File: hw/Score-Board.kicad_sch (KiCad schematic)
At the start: 102 parts, among them J1 Conn_01x03, J2 Conn_01x04, J3 Barrel_Jack, J4 Conn_01x04, J5 Conn_01x02, J6 DB25_Receptacle_MountingHoles, J7 Conn_01x10, J8 Conn_01x14, Q1 2N3905, Q10 2N3904, Q11 2N3905, Q12 2N3904, Q13 2N3905, Q14 2N3904, Q15 2N3905, Q16 2N3904, Q17 2N3905, Q18 2N3904, Q19 2N3905, Q2 2N3904, Q20 2N3904, Q21 2N3905, Q22 2N3904, Q3 2N3904, Q4 2N3904, Q5 2N3904, Q6 2N3904, Q7 2N3904, Q8 2N3904, Q9 2N3904, SW1 RESET, SW2 NETWORK, SW3 INPUT-SW, U1 PicoW, U2 E18-MS1-PCB, U3 TSOP382xx, U4 TSOP382xx

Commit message: Schematic complete v0.1. Ready for layout.
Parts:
- removed J5: Conn_01x02, symbol Connector_Generic:Conn_01x02
- removed R26, R27: 150, symbol Device:R_Small_US
- added C4, C5: 1.0uF, symbol Device:C
- added D2: DIODE SCHOTTKY 50V 200MA DO35, symbol Device:D_Schottky
- added J2: J-V12, symbol Connector_Generic:Conn_01x02
- added J3: J-VSYS, symbol Connector_Generic:Conn_01x02
- added J4: J-V3.3, symbol Connector_Generic:Conn_01x02
- added J5: MicroSD-Socket, symbol Connector:Micro_SD_Card_Det1
- added R27, R44: 150, symbol AES_Library:R_PWRSRC
- added TP1: Conn_01x01, symbol Connector_Generic:Conn_01x01
- added U5: MCP1702-5002E, Package_TO_SOT_THT:TO-92_Inline, symbol Regulator_Linear:MCP1700x-500xxTO
- renumbered J3 to J1, J7 to J10, J8 to J11, J1 to J6, J2 to J7, J4 to J8, J6 to J9
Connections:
- net +12V: now also R11.1, C4.1, J2.2 (Pin_2), U5.2 (VI)
- net +3.3V: now also J4.2 (Pin_2), J5.4 (VDD), R27.1 (I), R44.1 (I)
- net DD.IND: now also LED10.2 (A)
- net GND: now also J6.1 (Pin_1), C4.2, C5.2, J2.1 (Pin_1), J3.1 (Pin_1), J5.10 (SHIELD), J5.6 (VSS), U5.1 (GND); no longer J6.3 (Pin_3), LED2.1 (K), LED3.1 (K), U1.31 (GPIO26_ADC0), U2.12 (RUN_LED), U2.13 (NWK_LED)
- net SC_TX: now also J6.3 (Pin_3); no longer J6.1 (Pin_1)
- net SE.E: now also J5.5 (CLK)
- net SE.F: now also J5.3 (CMD)
- net SE.G: now also J5.7 (DAT0)
- net VIR.B: now reaches C2.2, U4.3 (Vs)
- net VIR.B: now also R27.2 (O)
- net VSYS: now reaches U1.39 (VSYS)
- net VSYS: now also D2.1 (K), J3.2 (Pin_2), J4.1 (Pin_1)
- net VIR.A: now reaches C3.2, U3.3 (Vs)
- net VIR.A: now also R44.2 (O)
- new net: LED3.1 (K), U2.13 (NWK_LED)
- new net: LED2.1 (K), U2.12 (RUN_LED)
- new net +5V: C5.1, D2.2 (A), TP1.1 (Pin_1), U5.3 (VO)
- new net SD_CS-: J5.2 (DAT3/CD), U1.31 (GPIO26_ADC0)
- no-connect marks 13 -> 20
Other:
- note added: "IR Receiver A"
- note added: "IR Receiver B"
- note removed: "SEGMENT DRIVE BUS (A-G,P)"
- note removed: "SEGMENT ENABLE BUS (A-G,P)"
- moved on the sheet: BZ1, C1, C2, C3, D1, J1, J6, J7, J8, LED1, LED2, LED3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

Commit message: Schematic updated with 3 digit boards
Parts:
- removed DIG1, DIG2, DIG3, DIG4: WJLEDS40012TUR11, Display_7Segment:SA15-11xxx, symbol AES_Library:WJ-LEDS40012TUR11
- removed DIG5, DIG6: WJLEDS18012TUR11, Display_7Segment:SA15-11xxx, symbol AES_Library:WJ-LEDS18012TUR11
- removed J10: Conn_01x10, symbol Connector_Generic:Conn_01x10
- removed J11: Conn_01x14, symbol Connector_Generic:Conn_01x14
- removed LED10: IND-B3, symbol Device:LED
- removed LED11: IND-B4, symbol Device:LED
- removed LED4: IND-A1, symbol Device:LED
- removed LED5: IND-A2, symbol Device:LED
- removed LED6: IND-A3, symbol Device:LED
- removed LED7: IND-A4, symbol Device:LED
- removed LED8: IND-B1, symbol Device:LED
- removed LED9: IND-B2, symbol Device:LED
- removed R28, R29, R30, R31, R32, R33, R34, R36, R37, R38, R39, R40, R41, R42: 150, symbol Device:R_Small_US
- removed R35, R43: 0, symbol Device:R_Small_US
- added H1, H2, H3, H4: MountingHole, MountingHole:MountingHole_3.2mm_M3, symbol Mechanical:MountingHole
- added J14: Conn_02x09_Odd_Even, symbol Connector_Generic:Conn_02x09_Odd_Even
- added J14: Screw_Terminal_01x02, symbol Connector:Screw_Terminal_01x02
- BZ1: footprint (none) -> MountingHole:MountingHole_3.2mm_M3
- C1: footprint (none) -> Capacitor_THT:CP_Radial_D8.0mm_P3.50mm
- C2: renamed from C4; footprint (none) -> Capacitor_THT:CP_Radial_D5.0mm_P2.00mm
- C3: renamed from C5; footprint (none) -> Capacitor_THT:CP_Radial_D5.0mm_P2.00mm
- C4: renamed from C3; footprint (none) -> Capacitor_THT:CP_Radial_D5.0mm_P2.00mm
- C5: renamed from C2; footprint (none) -> Capacitor_THT:CP_Radial_D5.0mm_P2.00mm
- D2: footprint (none) -> Diode_THT:D_DO-35_SOD27_P10.16mm_Horizontal
- J1: footprint (none) -> AES_Library:CUI_PJ-037B
- J10: renamed from J9; footprint (none) -> Connector_Dsub:DSUB-25_Female_Horizontal_P2.77x2.54mm_EdgePinOffset9.40mm
- J2: renamed from J7; footprint (none) -> Connector_PinHeader_2.54mm:PinHeader_1x04_P2.54mm_Vertical
- J3: renamed from J6; footprint (none) -> Connector_PinHeader_2.54mm:PinHeader_1x03_P2.54mm_Vertical
- J4: renamed from J8; footprint (none) -> Connector_PinHeader_2.54mm:PinHeader_1x04_P2.54mm_Vertical
- J5: footprint (none) -> AES_Library:GCT_MEM2075-00-140-01-A
- J6: renamed from J2; footprint (none) -> Connector_PinHeader_2.54mm:PinHeader_1x02_P2.54mm_Vertical
- J7: renamed from J3; footprint (none) -> Connector_PinHeader_2.54mm:PinHeader_1x02_P2.54mm_Vertical
- J8: renamed from J4; footprint (none) -> Connector_PinHeader_2.54mm:PinHeader_1x02_P2.54mm_Vertical
- LED1, LED2, LED3: footprint (none) -> LED_THT:LED_D5.0mm-3
- R1: renamed from R44; footprint (none) -> Resistor_THT:R_Axial_DIN0207_L6.3mm_D2.5mm_P10.16mm_Horizontal
- R10: renamed from R13; footprint (none) -> Resistor_THT:R_Axial_DIN0207_L6.3mm_D2.5mm_P10.16mm_Horizontal
- R11: renamed from R14; footprint (none) -> Resistor_THT:R_Axial_DIN0207_L6.3mm_D2.5mm_P10.16mm_Horizontal
- R12: renamed from R15; footprint (none) -> Resistor_THT:R_Axial_DIN0207_L6.3mm_D2.5mm_P10.16mm_Horizontal
- R13: renamed from R16; footprint (none) -> Resistor_THT:R_Axial_DIN0207_L6.3mm_D2.5mm_P10.16mm_Horizontal
- R14: renamed from R17; footprint (none) -> Resistor_THT:R_Axial_DIN0207_L6.3mm_D2.5mm_P10.16mm_Horizontal
- R15: renamed from R18; footprint (none) -> Resistor_THT:R_Axial_DIN0207_L6.3mm_D2.5mm_P10.16mm_Horizontal
- R16: renamed from R19; footprint (none) -> Resistor_THT:R_Axial_DIN0207_L6.3mm_D2.5mm_P10.16mm_Horizontal
- R17: renamed from R20; footprint (none) -> Resistor_THT:R_Axial_DIN0207_L6.3mm_D2.5mm_P10.16mm_Horizontal
- R18: renamed from R24; footprint (none) -> Resistor_THT:R_Axial_DIN0207_L6.3mm_D2.5mm_P10.16mm_Horizontal
- R19: renamed from R25; footprint (none) -> Resistor_THT:R_Axial_DIN0207_L6.3mm_D2.5mm_P10.16mm_Horizontal
- R2: renamed from R27; footprint (none) -> Resistor_THT:R_Axial_DIN0207_L6.3mm_D2.5mm_P10.16mm_Horizontal
- R20: renamed from R3; footprint (none) -> Resistor_THT:R_Axial_DIN0207_L6.3mm_D2.5mm_P10.16mm_Horizontal
- R3: renamed from R21; footprint (none) -> Resistor_THT:R_Axial_DIN0207_L6.3mm_D2.5mm_P10.16mm_Horizontal
- R33: renamed from R4; footprint (none) -> Resistor_THT:R_Axial_DIN0207_L6.3mm_D2.5mm_P10.16mm_Horizontal
- R34: renamed from R5; footprint (none) -> Resistor_THT:R_Axial_DIN0207_L6.3mm_D2.5mm_P10.16mm_Horizontal
- R39: renamed from R6; footprint (none) -> Resistor_THT:R_Axial_DIN0207_L6.3mm_D2.5mm_P10.16mm_Horizontal
- R4: renamed from R22; footprint (none) -> Resistor_THT:R_Axial_DIN0207_L6.3mm_D2.5mm_P10.16mm_Horizontal
- R40: renamed from R7; footprint (none) -> Resistor_THT:R_Axial_DIN0207_L6.3mm_D2.5mm_P10.16mm_Horizontal
- R41: renamed from R8; footprint (none) -> Resistor_THT:R_Axial_DIN0207_L6.3mm_D2.5mm_P10.16mm_Horizontal
- R42: renamed from R9; footprint (none) -> Resistor_THT:R_Axial_DIN0207_L6.3mm_D2.5mm_P10.16mm_Horizontal
- R43: renamed from R10; footprint (none) -> Resistor_THT:R_Axial_DIN0207_L6.3mm_D2.5mm_P10.16mm_Horizontal
- R5: renamed from R23; footprint (none) -> Resistor_THT:R_Axial_DIN0207_L6.3mm_D2.5mm_P10.16mm_Horizontal
- R6: renamed from R1; footprint (none) -> Resistor_THT:R_Axial_DIN0207_L6.3mm_D2.5mm_P10.16mm_Horizontal
- R7: renamed from R2; footprint (none) -> Resistor_THT:R_Axial_DIN0207_L6.3mm_D2.5mm_P10.16mm_Horizontal
- R8: renamed from R11; footprint (none) -> Resistor_THT:R_Axial_DIN0207_L6.3mm_D2.5mm_P10.16mm_Horizontal
- R9: renamed from R12; footprint (none) -> Resistor_THT:R_Axial_DIN0207_L6.3mm_D2.5mm_P10.16mm_Horizontal
- SW1, SW2, SW3: footprint (none) -> AES_Library:SW_TL1100F160Q
- TP1: footprint (none) -> Connector_PinHeader_2.54mm:PinHeader_1x01_P2.54mm_Vertical
- U1: footprint RPi_PicoW:RPi_Pico_SMD_TH -> AES_Library:RPi_PicoW_SMD_TH
- renumbered Q2 to Q1, Q13 to Q10, Q15 to Q11, Q17 to Q12, Q19 to Q13, Q21 to Q14, Q3 to Q15, Q4 to Q16, Q5 to Q17, Q6 to Q18, Q7 to Q19, Q12 to Q2, Q8 to Q20, Q9 to Q21, Q10 to Q22, Q14 to Q3, Q16 to Q4, Q18 to Q5, Q20 to Q6, Q22 to Q7, Q1 to Q8, Q11 to Q9
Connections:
- net +12V: now also J14.2 (Pin_2)
- net +3.3V: no longer U1.35 (ADC_VREF)
- net DD.A01: now also J10.20 (P20), J14.4 (Pin_4); no longer J10.7
- net DD.A10: now also J10.7, J14.2 (Pin_2); no longer J10.20 (P20)
- net DD.B01: now also J10.21 (P21), J14.8 (Pin_8); no longer J10.8
- net DD.B10: now also J10.8, J14.6 (Pin_6); no longer J10.21 (P21)
- net DD.C01: now also J10.22 (P22), J14.12 (Pin_12); no longer J10.9
- net DD.C10: now also J10.9, J14.10 (Pin_10); no longer J10.22 (P22)
- net DD.IND: now also J14.14 (Pin_14), J14.16 (Pin_16)
- net GND: now also J14.1 (Pin_1), J14.1 (Pin_1), J14.18 (Pin_18); no longer J10.13
- net SD.A: now also J14.3 (Pin_3)
- net SD.B: now also J14.5 (Pin_5)
- net SD.C: now also J14.7 (Pin_7)
- net SD.D: now also J14.9 (Pin_9)
- net SD.E: now also J14.11 (Pin_11)
- net SD.F: now also J14.13 (Pin_13)
- net SD.G: now also J14.15 (Pin_15)
- net SD.P: now also J14.17 (Pin_17)
- net BZR: now reaches BZ1.1 (-), U1.32 (GPIO27_ADC1)
- net BZR: now also J10.13
- no-connect marks 20 -> 21
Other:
- added sheet Digits Boards (digits.kicad_sch)
- moved on the sheet: BZ1, C1, D1, J10, J8

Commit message: Schematic updated with digit drive resistors
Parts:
- added H1, H4: MountingHole, MountingHole:MountingHole_3.2mm_M3, symbol Mechanical:MountingHole
- renumbered H1 to H2, H2 to H3, H3 to H5, H4 to H6
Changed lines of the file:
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@@
     (comment 1 "Copyright AESilky 2023")
   )
-  (bus_alias "SEGMENT-DRIVE-C" (members "SDC.A" "SDC.B" "SDC.C" "SDC.D" "SDC.E" "SDC.F" "SDC.G" "SDC.P"))
   (bus_alias "DIGIT-ENABLE" (members "DE.A10" "DE.A01" "DE.B10" "DE.B01" "DE.C10" "DE.C01" "DE.IND"))
-  (bus_alias "SEGMENT-ENABLE" (members "SE.A" "SE.B" "SE.C" "SE.D" "SE.E" "SE.F" "SE.G" "SE.P"))
   (bus_alias "SEGMENT-DRIVE" (members "SD.A" "SD.B" "SD.C" "SD.D" "SD.E" "SD.F" "SD.G" "SD.P"))
   (bus_alias "DIGIT-DRIVE" (members "DD.A10" "DD.A01" "DD.B10" "DD.B01" "DD.C10" "DD.C01" "DD.IND"))
+  (bus_alias "SEGMENT-ENABLE" (members "SE.A" "SE.B" "SE.C" "SE.D" "SE.E" "SE.F" "SE.G" "SE.P"))
+  (bus_alias "SEGMENT-DRIVE-C" (members "SDC.A" "SDC.B" "SDC.C" "SDC.D" "SDC.E" "SDC.F" "SDC.G" "SDC.P"))
   (junction (at 116.84 158.75) (diameter 0) (color 0 0 0 0)
   )
@@
     )
   )
+  (symbol (lib_id "Mechanical:MountingHole") (at 254 251.46 0) (unit 1)
+    (in_bom yes) (on_board yes) (dnp no)
+    (property "Reference" "H4" (at 256.54 250.825 0)
+      (effects (font (size 1.27 1.27)) (justify left))
+    )
+    (property "Value" "MountingHole" (at 247.65 255.27 0)
+      (effects (font (size 1.27 1.27)) (justify left))
+    )
+    (property "Footprint" "MountingHole:MountingHole_3.2mm_M3" (at 254 251.46 0)
+      (effects (font (size 1.27 1.27)) hide)
+    )
+    (property "Datasheet" "~" (at 254 251.46 0)
+      (effects (font (size 1.27 1.27)) hide)
+    )
+    (instances
+      (project "Score-Board"
+        (path "/68d67001-ae41-4f9d-ab97-8e1f3faa3aca"
+          (reference "H4") (unit 1)
+        )
+      )
+    )
+  )
   (symbol (lib_id "Device:R_Small_US") (at 175.26 137.16 0) (unit 1)
     (in_bom yes) (on_board yes) (dnp no) (fields_autoplaced)
@@
     )
   )
+  (symbol (lib_id "Mechanical:MountingHole") (at 254 241.3 0) (unit 1)
+    (in_bom yes) (on_board yes) (dnp no)
+    (property "Reference" "H1" (at 256.54 240.665 0)
+      (effects (font (size 1.27 1.27)) (justify left))
+    )
+    (property "Value" "MountingHole" (at 247.65 245.11 0)
+      (effects (font (size 1.27 1.27)) (justify left))
+    )
+    (property "Footprint" "MountingHole:MountingHole_3.2mm_M3" (at 254 241.3 0)
+      (effects (font (size 1.27 1.27)) hide)
+    )
+    (property "Datasheet" "~" (at 254 241.3 0)
+      (effects (font (size 1.27 1.27)) hide)
+    )
+    (instances
+      (project "Score-Board"
+        (path "/68d67001-ae41-4f9d-ab97-8e1f3faa3aca"
+          (reference "H1") (unit 1)
+        )
+      )
+    )
+  )
   (symbol (lib_id "Mechanical:MountingHole") (at 271.78 251.46 0) (unit 1)
     (in_bom yes) (on_board yes) (dnp no)
-    (property "Reference" "H3" (at 274.32 250.825 0)
+    (property "Reference" "H5" (at 274.32 250.825 0)
       (effects (font (size 1.27 1.27)) (justify left))
     )
@@
       (project "Score-Board"
         (path "/68d67001-ae41-4f9d-ab97-8e1f3faa3aca"
-          (reference "H3") (unit 1)
+          (reference "H5") (unit 1)
         )
       )
@@
   (symbol (lib_id "Mechanical:MountingHole") (at 288.29 241.3 0) (unit 1)
     (in_bom yes) (on_board yes) (dnp no)
-    (property "Reference" "H2" (at 290.83 240.665 0)
+    (property "Reference" "H3" (at 290.83 240.665 0)
       (effects (font (size 1.27 1.27)) (justify left))
     )
@@
       (project "Score-Board"
         (path "/68d67001-ae41-4f9d-ab97-8e1f3faa3aca"
-          (reference "H2") (unit 1)
+          (reference "H3") (unit 1)
         )
       )
@@
   (symbol (lib_id "Mechanical:MountingHole") (at 271.78 241.3 0) (unit 1)
     (in_bom yes) (on_board yes) (dnp no)
-    (property "Reference" "H1" (at 274.32 240.665 0)
+    (property "Reference" "H2" (at 274.32 240.665 0)
       (effects (font (size 1.27 1.27)) (justify left))
     )
@@
       (project "Score-Board"
         (path "/68d67001-ae41-4f9d-ab97-8e1f3faa3aca"
-          (reference "H1") (unit 1)
+          (reference "H2") (unit 1)
         )
       )
@@
   (symbol (lib_id "Mechanical:MountingHole") (at 288.29 251.46 0) (unit 1)
     (in_bom yes) (on_board yes) (dnp no)
-    (property "Reference" "H4" (at 290.83 250.825 0)
+    (property "Reference" "H6" (at 290.83 250.825 0)
       (effects (font (size 1.27 1.27)) (justify left))
     )
@@
       (project "Score-Board"
         (path "/68d67001-ae41-4f9d-ab97-8e1f3faa3aca"
-          (reference "H4") (unit 1)
+          (reference "H6") (unit 1)
         )
       )

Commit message: Footprints assigned
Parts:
- J14: footprint (none) -> Connector_PinHeader_2.54mm:PinHeader_2x09_P2.54mm_Vertical
- J14: footprint (none) -> TerminalBlock_Philmore:TerminalBlock_Philmore_TB132_1x02_P5.00mm_Horizontal
- U2: footprint (none) -> AES_Library:E18-MS1-PCB-AES
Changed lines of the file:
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@@
       (effects (font (size 1.27 1.27)) hide)
     )
-    (property "Footprint" "" (at 232.41 92.71 0)
+    (property "Footprint" "Connector_PinHeader_2.54mm:PinHeader_2x09_P2.54mm_Vertical" (at 232.41 92.71 0)
       (effects (font (size 1.27 1.27)) hide)
     )
@@
       (effects (font (size 1.27 1.27)))
     )
-    (property "Footprint" "" (at 96.52 163.83 0)
+    (property "Footprint" "AES_Library:E18-MS1-PCB-AES" (at 96.52 163.83 0)
       (effects (font (size 1.27 1.27)) hide)
     )
@@
       (effects (font (size 1.27 1.27)) hide)
     )
-    (property "Footprint" "" (at 48.26 24.13 0)
-      (effects (font (size 1.27 1.27)) hide)
-    )
+    (property "Footprint" "TerminalBlock_Philmore:TerminalBlock_Philmore_TB132_1x02_P5.00mm_Horizontal" (at 48.26 24.13 0)
+      (effects (font (size 1.27 1.27)) hide)
+    )

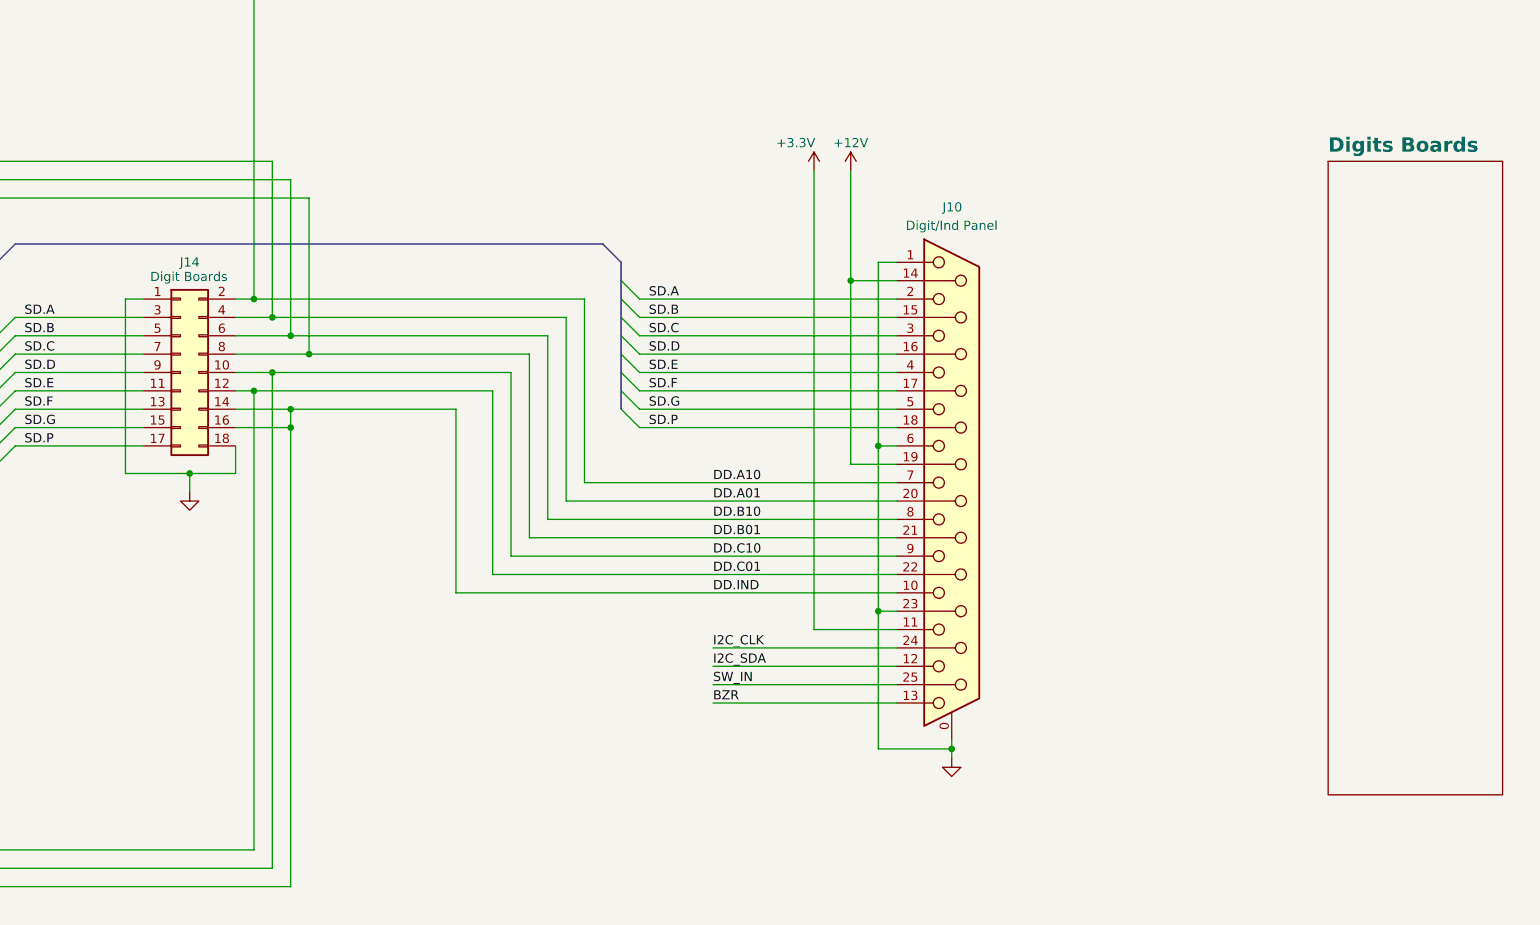
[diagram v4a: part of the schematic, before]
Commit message: Separate Main and Digits projects
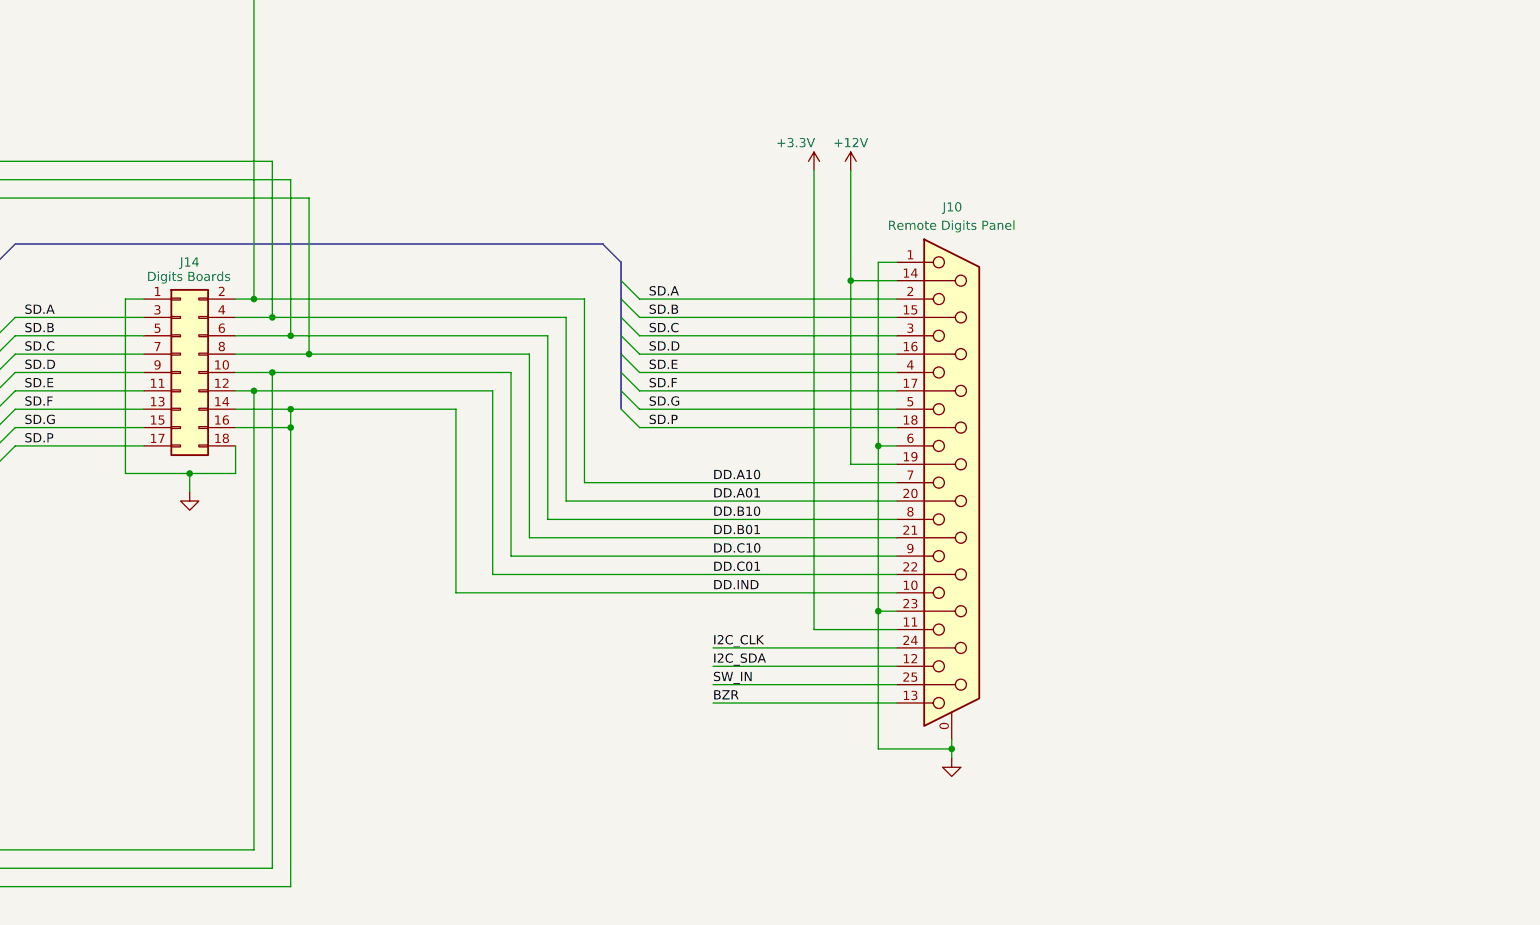
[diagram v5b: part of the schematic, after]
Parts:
- J10: Ref Digit/Ind Panel -> Remote Digits Panel
- J14: Ref Digit Boards -> Digits Boards
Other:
- removed sheet Digits Boards
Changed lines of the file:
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@@
     (comment 1 "Copyright AESilky 2023")
   )
-  (bus_alias "DIGIT-ENABLE" (members "DE.A10" "DE.A01" "DE.B10" "DE.B01" "DE.C10" "DE.C01" "DE.IND"))
-  (bus_alias "SEGMENT-DRIVE" (members "SD.A" "SD.B" "SD.C" "SD.D" "SD.E" "SD.F" "SD.G" "SD.P"))
-  (bus_alias "DIGIT-DRIVE" (members "DD.A10" "DD.A01" "DD.B10" "DD.B01" "DD.C10" "DD.C01" "DD.IND"))
-  (bus_alias "SEGMENT-ENABLE" (members "SE.A" "SE.B" "SE.C" "SE.D" "SE.E" "SE.F" "SE.G" "SE.P"))
   (bus_alias "SEGMENT-DRIVE-C" (members "SDC.A" "SDC.B" "SDC.C" "SDC.D" "SDC.E" "SDC.F" "SDC.G" "SDC.P"))
+  (bus_alias "SEGMENT-ENABLE" (members "SE.A" "SE.B" "SE.C" "SE.D" "SE.E" "SE.F" "SE.G" "SE.P"))
+  (bus_alias "DIGIT-DRIVE" (members "DD.A10" "DD.A01" "DD.B10" "DD.B01" "DD.C10" "DD.C01" "DD.IND"))
+  (bus_alias "SEGMENT-DRIVE" (members "SD.A" "SD.B" "SD.C" "SD.D" "SD.E" "SD.F" "SD.G" "SD.P"))
+  (bus_alias "DIGIT-ENABLE" (members "DE.A10" "DE.A01" "DE.B10" "DE.B01" "DE.C10" "DE.C01" "DE.IND"))
   (junction (at 116.84 158.75) (diameter 0) (color 0 0 0 0)
   )
@@
       (effects (font (size 1.27 1.27)) hide)
     )
-    (property "Ref" "Digit Boards" (at 233.5671 79.4662 0)
+    (property "Ref" "Digits Boards" (at 233.5671 79.4662 0)
       (effects (font (size 1.27 1.27)))
     )
@@
     (instances
       (project "Score-Board"
-        (path "/68d67001-ae41-4f9d-ab97-8e1f3faa3aca/09f2d907-5c8a-4b59-8f07-76f8dfe4c1bb"
-          (reference "J14") (unit 1)
-        )
         (path "/68d67001-ae41-4f9d-ab97-8e1f3faa3aca"
           (reference "J9") (unit 1)
@@
       (effects (font (size 1.27 1.27)) hide)
     )
-    (property "Ref" "Digit/Ind Panel" (at 339.09 72.39 0)
+    (property "Ref" "Remote Digits Panel" (at 339.09 72.39 0)
       (effects (font (size 1.27 1.27)))
     )
@@
       )
     )
-  )
-  (sheet (at 391.16 63.5) (size 24.13 87.63) (fields_autoplaced)
-    (stroke (width 0.1524) (type solid) (color 132 0 0 1))
-    (fill (color 255 255 194 1.0000))
-    (property "Sheetname" "Digits Boards" (at 391.16 62.4234 0)
-      (effects (font (size 2 2) bold) (justify left bottom))
-    )
-    (property "Sheetfile" "digits.kicad_sch" (at 391.16 151.7146 0)
-      (effects (font (size 1.27 1.27)) (justify left top) hide)
-    )
-    (instances
-      (project "Score-Board"
-        (path "/68d67001-ae41-4f9d-ab97-8e1f3faa3aca" (page "2"))
-      )
-    )
